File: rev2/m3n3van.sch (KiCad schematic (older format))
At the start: 116 parts, among them SW1 SW_Push, U1 SRV05-4, U2 ATmega32U4-AU, Y1 Resonator_Small

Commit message: Update rev2 for production
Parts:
- C7: footprint Capacitor_SMD:C_0603_1608Metric -> Capacitor_SMD:C_0402_1005Metric
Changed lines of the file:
@@
 F 0 "C7" H 9092 9446 50  0000 L CNN
 F 1 "10uF" H 9092 9355 50  0000 L CNN
-F 2 "Capacitor_SMD:C_0603_1608Metric" H 9000 9400 50  0001 C CNN
+F 2 "Capacitor_SMD:C_0402_1005Metric" H 9000 9400 50  0001 C CNN
 F 3 "~" H 9000 9400 50  0001 C CNN
 	1    9000 9400

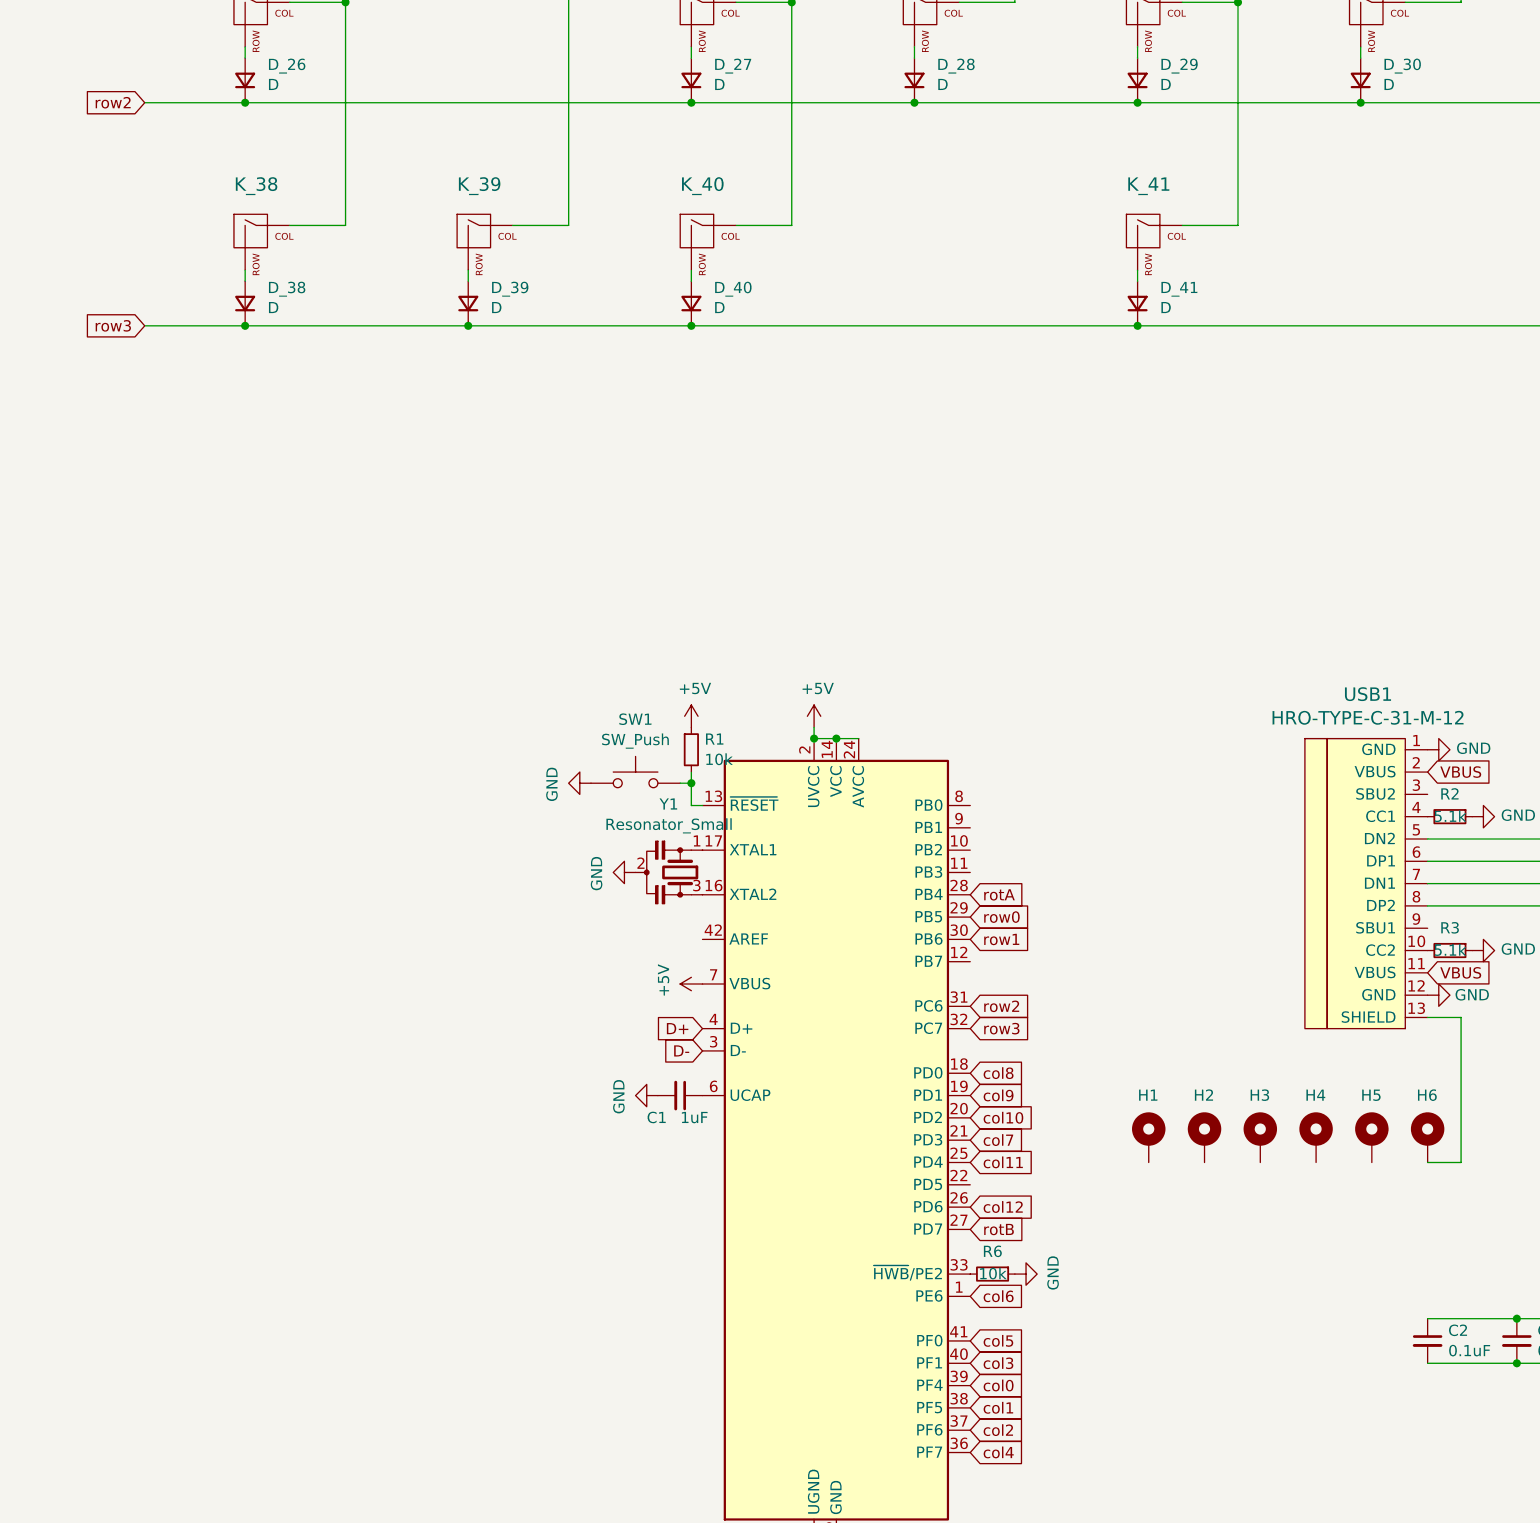
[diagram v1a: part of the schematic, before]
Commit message: Add second encoder, RGB header, switch to assembly resonator footprint
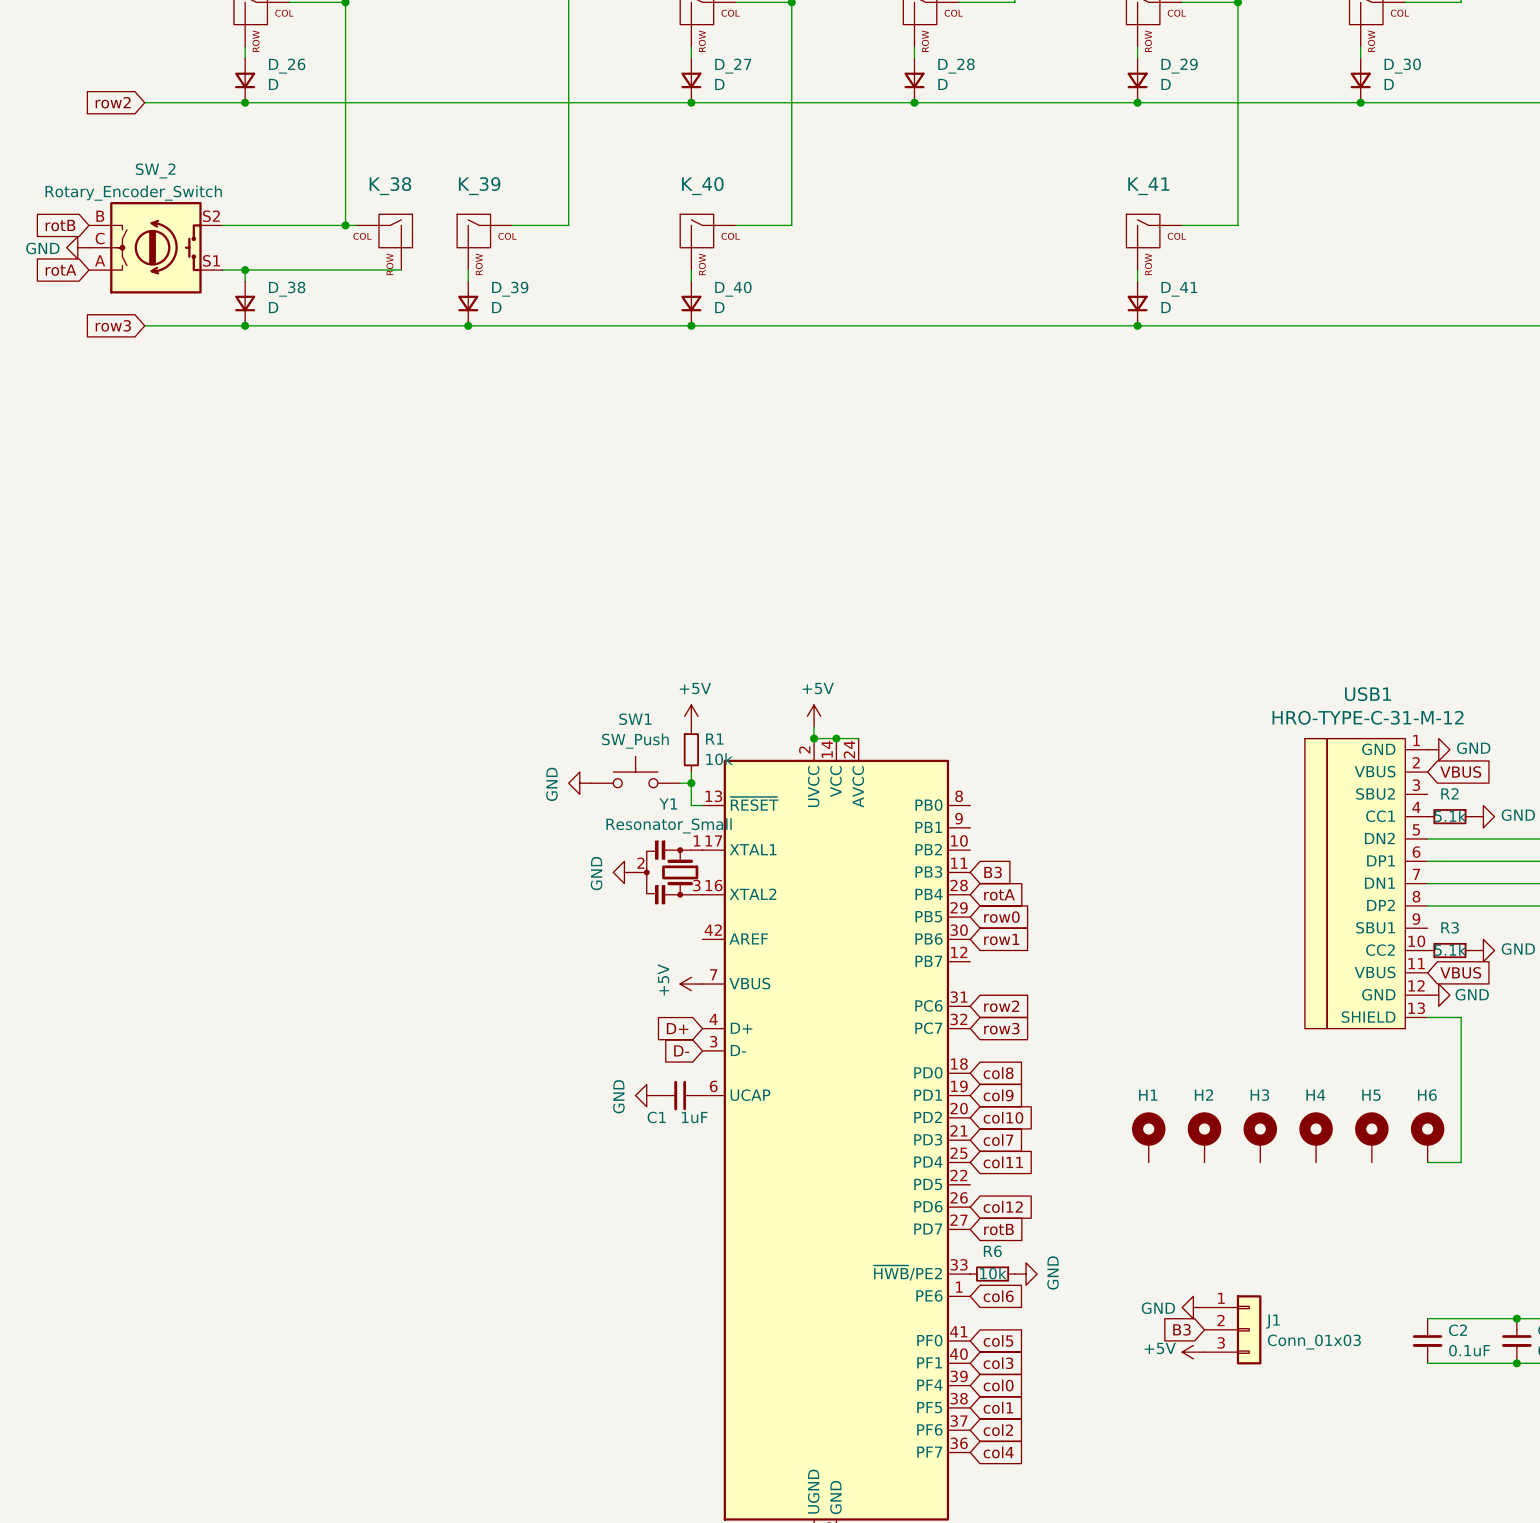
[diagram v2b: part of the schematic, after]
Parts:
- added J1: Conn_01x03, Connector_PinHeader_2.54mm:PinHeader_1x03_P2.54mm_Vertical, symbol Connector_Generic:Conn_01x03
- added SW_2: Rotary_Encoder_Switch, Rotary_Encoder:RotaryEncoder_Alps_EC11E-Switch_Vertical_H20mm, symbol Device:Rotary_Encoder_Switch
- Y1: footprint Crystal:Resonator_SMD_muRata_CSTxExxV-3Pin_3.0x1.1mm_HandSoldering -> Crystal:Resonator_SMD_muRata_CSTxExxV-3Pin_3.0x1.1mm
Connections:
- net +5V: now also J1.3 (Pin_3)
- net GND: now also J1.1 (Pin_1), SW_2.C
- net col0: now also SW_2.S2
- net rotA: now also SW_2.A
- net rotB: now also SW_2.B
- net at D_38.2 (A), K_38.2 (ROW): now also SW_2.S1
- net B3: now reaches U2.11 (PB3)
- net B3: now also J1.2 (Pin_2)
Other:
- moved on the sheet: K_38
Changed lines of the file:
@@
 	1250 4850 1700 4850
-$Comp
-L MX_Alps_Hybrid:MX-NoLED K_38
-U 1 1 00000381
-P 1750 4450
-F 0 "K_38" H 1750 4683 60  0000 C CNN
-F 1 "KEYSW" H 1750 4350 60  0001 C CNN
-F 2 "MX_Only:MXOnly-1U-NoLED" H 1750 4450 60  0001 C CNN
-F 3 "" H 1750 4450 60  0000 C CNN
-	1    1750 4450
-	1    0    0    -1
-$EndComp
 $Comp
 L Device:D_Small D_38
@@
 	0    -1   -1   0
 $EndComp
-Wire Wire Line
-	1900 4400 2150 4400
-Wire Wire Line
-	1700 4600 1700 4650
 Connection ~ 1700 4850
 $Comp
@@
 F 0 "Y1" V 3345 7250 50  0000 C CNN
 F 1 "Resonator_Small" V 3436 7250 50  0000 C CNN
-F 2 "Crystal:Resonator_SMD_muRata_CSTxExxV-3Pin_3.0x1.1mm_HandSoldering" H 3625 7300 50  0001 C CNN
+F 2 "Crystal:Resonator_SMD_muRata_CSTxExxV-3Pin_3.0x1.1mm" H 3625 7300 50  0001 C CNN
 F 3 "~" H 3625 7300 50  0001 C CNN
 	1    3650 7300
@@
 Text GLabel 4950 8600 2    50   Input ~ 0
 col11
+$Comp
+L Device:Rotary_Encoder_Switch SW_2
+U 1 1 60523F15
+P 1300 4500
+F 0 "SW_2" H 1300 4150 50  0000 C CNN
+F 1 "Rotary_Encoder_Switch" H 1200 4250 50  0000 C CNN
+F 2 "Rotary_Encoder:RotaryEncoder_Alps_EC11E-Switch_Vertical_H20mm" H 1150 4660 50  0001 C CNN
+F 3 "~" H 1300 4760 50  0001 C CNN
+	1    1300 4500
+	1    0    0    1
+$EndComp
+Wire Wire Line
+	2200 4400 2150 4400
+$Comp
+L MX_Alps_Hybrid:MX-NoLED K_38
+U 1 1 00000381
+P 2350 4450
+F 0 "K_38" H 2350 4683 60  0000 C CNN
+F 1 "KEYSW" H 2350 4350 60  0001 C CNN
+F 2 "MX_Only:MXOnly-1U-NoLED" H 2350 4450 60  0001 C CNN
+F 3 "" H 2350 4450 60  0000 C CNN
+	1    2350 4450
+	-1   0    0    -1
+$EndComp
+Wire Wire Line
+	1600 4400 2150 4400
+Connection ~ 2150 4400
+Wire Wire Line
+	2400 4600 1700 4600
+Wire Wire Line
+	1700 4650 1700 4600
+Connection ~ 1700 4600
+Wire Wire Line
+	1700 4600 1600 4600
+$Comp
+L power:GND #PWR0102
+U 1 1 605DA9D5
+P 1000 4500
+F 0 "#PWR0102" H 1000 4250 50  0001 C CNN
+F 1 "GND" V 1005 4372 50  0000 R CNN
+F 2 "" H 1000 4500 50  0001 C CNN
+F 3 "" H 1000 4500 50  0001 C CNN
+	1    1000 4500
+	0    1    1    0
+$EndComp
+Text GLabel 1000 4600 0    50   Input ~ 0
+rotA
+Text GLabel 1000 4400 0    50   Input ~ 0
+rotB
+$Comp
+L Connector_Generic:Conn_01x03 J1
+U 1 1 60649448
+P 6200 9350
+F 0 "J1" H 6280 9392 50  0000 L CNN
+F 1 "Conn_01x03" H 6280 9301 50  0000 L CNN
+F 2 "Connector_PinHeader_2.54mm:PinHeader_1x03_P2.54mm_Vertical" H 6200 9350 50  0001 C CNN
+F 3 "~" H 6200 9350 50  0001 C CNN
+	1    6200 9350
+	1    0    0    -1
+$EndComp
+$Comp
+L power:GND #PWR0103
+U 1 1 6064FD44
+P 6000 9250
+F 0 "#PWR0103" H 6000 9000 50  0001 C CNN
+F 1 "GND" V 6005 9122 50  0000 R CNN
+F 2 "" H 6000 9250 50  0001 C CNN
+F 3 "" H 6000 9250 50  0001 C CNN
+	1    6000 9250
+	0    1    1    0
+$EndComp
+$Comp
+L power:+5V #PWR0104
+U 1 1 60650D5A
+P 6000 9450
+F 0 "#PWR0104" H 6000 9300 50  0001 C CNN
+F 1 "+5V" V 6015 9578 50  0000 L CNN
+F 2 "" H 6000 9450 50  0001 C CNN
+F 3 "" H 6000 9450 50  0001 C CNN
+	1    6000 9450
+	0    -1   -1   0
+$EndComp
+Text GLabel 6000 9350 0    50   Input ~ 0
+B3
+Text GLabel 4950 7300 2    50   Input ~ 0
+B3
 $EndSCHEMATC

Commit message: Update components, production files
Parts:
- C7: footprint Capacitor_SMD:C_0402_1005Metric -> Capacitor_SMD:C_0603_1608Metric
- D_1, D_10, D_11, D_12, D_13, D_14, D_15, D_16, D_17, D_18, D_19, D_2, D_20, D_21, D_22, D_23, D_24, D_25, D_26, D_27, D_28, D_29, D_3, D_30, D_31, D_32, D_33, D_34, D_35, D_36, D_37, D_38, D_39, D_4, D_40, D_41, D_42, D_43, D_44, D_45, D_5, D_6, D_7, D_8, D_9: footprint Diode_SMD:D_0603_1608Metric -> Diode_SMD:D_SOD-123

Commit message: Switch to crystal, add MU dual footprint
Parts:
- removed Y1: Resonator_Small, Crystal:Resonator_SMD_muRata_CSTxExxV-3Pin_3.0x1.1mm, symbol Device:Resonator_Small
- added C8, C9: 22pF, Capacitor_SMD:C_0603_1608Metric, symbol Device:C_Small
- added U3: ATmega32U4-MU, Package_DFN_QFN:QFN-44-1EP_7x7mm_P0.5mm_EP5.2x5.2mm, symbol MCU_Microchip_ATmega:ATmega32U4-MU
- added Y1: 16MHz, Crystal:Crystal_SMD_3225-4Pin_3.2x2.5mm, symbol Device:Crystal_GND24_Small
- U2: symbol MCU_Microchip_ATmega:ATmega32U4-AU -> m3n3van-rescue:ATmega32U4-AU-MCU_Microchip_ATmega
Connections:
- net +5V: now also U3.14 (VCC), U3.2 (UVCC), U3.24 (AVCC), U3.34 (VCC), U3.44 (AVCC), U3.7 (VBUS)
- net B3: now also U3.11 (PB3)
- net D+: now also U3.4 (D+)
- net D-: now also U3.3 (D-)
- net GND: now also C8.2, C9.1, U3.15 (GND), U3.23 (GND), U3.35 (GND), U3.43 (GND), U3.45 (GND), U3.5 (UGND), Y1.2, Y1.4
- net col0: now also U3.39 (PF4)
- net col1: now also U3.38 (PF5)
- net col10: now also U3.20 (PD2)
- net col11: now also U3.25 (PD4)
- net col12: now also U3.26 (PD6)
- net col2: now also U3.37 (PF6)
- net col3: now also U3.40 (PF1)
- net col4: now also U3.36 (PF7)
- net col5: now also U3.41 (PF0)
- net col6: now also U3.1 (PE6)
- net col7: now also U3.21 (PD3)
- net col8: now also U3.18 (PD0)
- net col9: now also U3.19 (PD1)
- net rotA: now also U3.28 (PB4)
- net rotB: now also U3.27 (PD7)
- net row0: now also U3.29 (PB5)
- net row1: now also U3.30 (PB6)
- net row2: now also U3.31 (PC6)
- net row3: now also U3.32 (PC7)
- net at U2.10 (PB2): now also U3.10 (PB2)
- net at U2.12 (PB7): now also U3.12 (PB7)
- net at R1.2, SW1.2, U2.13 (~RESET): now also U3.13 (~RESET)
- net at U2.16 (XTAL2): now also C9.2, U3.16 (XTAL2), Y1.3
- net at U2.17 (XTAL1): now also C8.1, U3.17 (XTAL1), Y1.1
- net at U2.22 (PD5): now also U3.22 (PD5)
- net at R6.2, U2.33 (~HWB~/PE2): now also U3.33 (~HWB~/PE2)
- net at U2.42 (AREF): now also U3.42 (AREF)
- net at C1.1, U2.6 (UCAP): now also U3.6 (UCAP)
- net at U2.8 (PB0): now also U3.8 (PB0)
- net at U2.9 (PB1): now also U3.9 (PB1)
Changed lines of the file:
@@
 EESchema Schematic File Version 4
-LIBS:m3n3van-cache
 EELAYER 30 0
 EELAYER END
@@
 $EndComp
 $Comp
-L MCU_Microchip_ATmega:ATmega32U4-AU U2
+L m3n3van-rescue:ATmega32U4-AU-MCU_Microchip_ATmega U2
 U 1 1 5FA094EE
 P 4350 8500
@@
 L power:GND #PWR06
 U 1 1 5FA09545
-P 3450 7300
+P 2800 7300
 AR Path="/5FA09545" Ref="#PWR06"  Part="1"
 AR Path="/5F9D2B6A/5FA09545" Ref="#PWR?"  Part="1"
-F 0 "#PWR06" H 3450 7050 50  0001 C CNN
-F 1 "GND" H 3455 7127 50  0000 C CNN
-F 2 "" H 3450 7300 50  0001 C CNN
-F 3 "" H 3450 7300 50  0001 C CNN
-	1    3450 7300
+F 0 "#PWR06" H 2800 7050 50  0001 C CNN
+F 1 "GND" H 2805 7127 50  0000 C CNN
+F 2 "" H 2800 7300 50  0001 C CNN
+F 3 "" H 2800 7300 50  0001 C CNN
+	1    2800 7300
 	0    1    1    0
 $EndComp
@@
 	8700 8450 8850 8450
 Connection ~ 8850 8450
-$Comp
-L Device:Resonator_Small Y1
-U 1 1 602FB621
-P 3650 7300
-F 0 "Y1" V 3345 7250 50  0000 C CNN
-F 1 "Resonator_Small" V 3436 7250 50  0000 C CNN
-F 2 "Crystal:Resonator_SMD_muRata_CSTxExxV-3Pin_3.0x1.1mm" H 3625 7300 50  0001 C CNN
-F 3 "~" H 3625 7300 50  0001 C CNN
-	1    3650 7300
-	0    1    1    0
-$EndComp
 $Comp
 L power:GND #PWR017
@@
 Text GLabel 4950 7300 2    50   Input ~ 0
 B3
+$Comp
+L MCU_Microchip_ATmega:ATmega32U4-MU U3
+U 1 1 61AD5AD1
+P 4350 8500
+F 0 "U3" H 4350 6611 50  0000 C CNN
+F 1 "ATmega32U4-MU" H 4350 6520 50  0000 C CNN
+F 2 "Package_DFN_QFN:QFN-44-1EP_7x7mm_P0.5mm_EP5.2x5.2mm" H 4350 8500 50  0001 C CIN
+F 3 "http://ww1.microchip.com/downloads/en/DeviceDoc/Atmel-7766-8-bit-AVR-ATmega16U4-32U4_Datasheet.pdf" H 4350 8500 50  0001 C CNN
+	1    4350 8500
+	1    0    0    -1
+$EndComp
+Connection ~ 3750 7000
+Connection ~ 4350 10300
+Connection ~ 4450 6700
+Connection ~ 4950 9100
+Connection ~ 3750 8300
+Connection ~ 3750 7800
+$Comp
+L Device:Crystal_GND24_Small Y1
+U 1 1 61B2CFAC
+P 3350 7300
+F 0 "Y1" V 3304 7444 50  0000 L CNN
+F 1 "16MHz" V 3395 7444 50  0000 L CNN
+F 2 "Crystal:Crystal_SMD_3225-4Pin_3.2x2.5mm" H 3350 7300 50  0001 C CNN
+F 3 "~" H 3350 7300 50  0001 C CNN
+	1    3350 7300
+	0    1    1    0
+$EndComp
+Wire Wire Line
+	3750 7200 3350 7200
+Connection ~ 3750 7200
+Connection ~ 3350 7200
+Wire Wire Line
+	3350 7200 3000 7200
+Wire Wire Line
+	3750 7400 3350 7400
+Connection ~ 3750 7400
+Connection ~ 3350 7400
+$Comp
+L Device:C_Small C8
+U 1 1 61B4F86C
+P 2900 7200
+F 0 "C8" V 2671 7200 50  0000 C CNN
+F 1 "22pF" V 2762 7200 50  0000 C CNN
+F 2 "Capacitor_SMD:C_0603_1608Metric" H 2900 7200 50  0001 C CNN
+F 3 "~" H 2900 7200 50  0001 C CNN
+	1    2900 7200
+	0    1    1    0
+$EndComp
+$Comp
+L Device:C_Small C9
+U 1 1 61B703CE
+P 2900 7400
+F 0 "C9" V 2700 7400 50  0000 C CNN
+F 1 "22pF" V 2800 7400 50  0000 C CNN
+F 2 "Capacitor_SMD:C_0603_1608Metric" H 2900 7400 50  0001 C CNN
+F 3 "~" H 2900 7400 50  0001 C CNN
+	1    2900 7400
+	0    -1   -1   0
+$EndComp
+Wire Wire Line
+	3000 7400 3350 7400
+Wire Wire Line
+	3450 7300 3250 7300
+Connection ~ 3250 7300
+Wire Wire Line
+	3250 7300 2800 7300
+Wire Wire Line
+	2800 7200 2800 7300
+Connection ~ 2800 7300
+Wire Wire Line
+	2800 7300 2800 7400
 $EndSCHEMATC
